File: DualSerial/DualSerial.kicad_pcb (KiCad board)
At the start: 2 copper layers, 99.9 x 99.9 mm, 7 parts, among them J1 IDE_CONNECTOR, J2 CF Adapter Power, J3 Bus_ISA_8bit

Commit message: DualSerial: More WIP on PCB layout.
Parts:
- removed MH1, MH2, MH3, MH4: MH, MountingHole:MountingHole_3.5mm_Pad
- added C1: 0.1uF, Capacitor_THT:C_Disc_D5.1mm_W3.2mm_P5.00mm, F.Cu at (162.6, 73.7)
- added C2: 0.1uF, Capacitor_THT:C_Disc_D5.1mm_W3.2mm_P5.00mm, F.Cu at (114.3, 69.8)
- added C3: 0.1uF, Capacitor_THT:C_Disc_D5.1mm_W3.2mm_P5.00mm, F.Cu at (186.1, 99.1)
- added C4: 0.1uF, Capacitor_THT:C_Disc_D5.1mm_W3.2mm_P5.00mm, F.Cu at (161.9, 48.3)
- added C5: 22uF, Capacitor_THT:CP_Radial_D7.5mm_P2.50mm, F.Cu at (179.1, 127.0)
- added C6: 4.7uF, Capacitor_THT:CP_Radial_D7.5mm_P2.50mm, F.Cu at (183.5, 89.5)
- added C7: 4.7uF, Capacitor_THT:CP_Radial_D7.5mm_P2.50mm, F.Cu at (174.6, 89.5)
- added C8: 0.1uF, Capacitor_THT:C_Disc_D5.1mm_W3.2mm_P5.00mm, F.Cu at (141.6, 48.3)
- added C9: 0.1uF, Capacitor_THT:C_Disc_D5.1mm_W3.2mm_P5.00mm, F.Cu at (181.6, 56.5)
- added CN1: DB9 Male, w_conn_d-sub:DB_9M, F.Cu at (196.7, 118.3)
- added CN2: DB9 Male, w_conn_d-sub:DB_9M, F.Cu at (196.7, 70.3)
- added J3: COM_A_SELECT, 00Custom:PinHeader_3x02_P2.54mm_Vertical, F.Cu at (110.5, 117.5)
- added J4: IRQ_B_SELECT, Connector_PinHeader_2.54mm:PinHeader_2x05_P2.54mm_Vertical, F.Cu at (124.5, 109.9)
- added U1: 16550/16C550, Package_DIP:DIP-40_W15.24mm_Socket, F.Cu at (143.5, 73.7)
- added U2: GAL16V8, Package_DIP:DIP-20_W7.62mm_Socket, F.Cu at (108.0, 73.7)
- added U3: GD75232N, Package_DIP:DIP-20_W7.62mm_Socket, F.Cu at (175.3, 99.1)
- added U4: 1.8432 MHz, 00Custom:Crystal_DIP8_DIP14, F.Cu at (148.6, 49.5)
- added U8: 16550/16C550, Package_DIP:DIP-40_W15.24mm_Socket, F.Cu at (121.9, 48.3)
- added U9: GD75232N, Package_DIP:DIP-20_W7.62mm_Socket, F.Cu at (175.3, 59.7)
- J1: value IDE_CONNECTOR -> COM_A_SELECT; footprint Connector_PinSocket_2.54mm:PinSocket_2x20_P2.54mm_Vertical -> 00Custom:PinHeader_3x02_P2.54mm_Vertical
- J2: value CF Adapter Power -> IRQ_A_SELECT; footprint Connector_PinHeader_2.54mm:PinHeader_1x02_P2.54mm_Vertical -> Connector_PinHeader_2.54mm:PinHeader_2x05_P2.54mm_Vertical
- moved J1 76.0 mm to (110.5, 109.9)
- moved J2 64.7 mm to (133.3, 109.9), turned to 0 degrees
- renumbered J3 to J5
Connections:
- net -5V renamed Net-(J5-Pad5)
- net A10 renamed Net-(J5-Pad52)
- net A11 renamed Net-(J5-Pad51)
- net A12 renamed Net-(J5-Pad50)
- net A13 renamed Net-(J5-Pad49)
- net A14 renamed Net-(J5-Pad48)
- net A15 renamed Net-(J5-Pad47)
- net A16 renamed Net-(J5-Pad46)
- net A17 renamed Net-(J5-Pad45)
- net A18 renamed Net-(J5-Pad44)
- net A19 renamed Net-(J5-Pad43)
- net ALE renamed Net-(J5-Pad28)
- net CLK renamed Net-(J5-Pad20)
- net DRQ1 renamed Net-(J5-Pad18)
- net DRQ2 renamed Net-(J5-Pad6)
- net DRQ3 renamed Net-(J5-Pad16)
- net IOCHRDY renamed Net-(J5-Pad41)
- net IRQ6 renamed Net-(J5-Pad22)
- net OSC renamed Net-(J5-Pad30)
- net TC renamed Net-(J5-Pad27)
- net ~DACK0 renamed Net-(J5-Pad19)
- net ~DACK1 renamed Net-(J5-Pad17)
- net ~DACK2 renamed Net-(J5-Pad26)
- net ~DACK3 renamed Net-(J5-Pad15)
- net ~IO_CH_CK renamed Net-(J5-Pad32)
- net ~MEMR renamed Net-(J5-Pad12)
- net ~MEMW renamed Net-(J5-Pad11)
- J1 pad 1: Net-(J1-Pad1) -> VCC
- J1 pad 3: Net-(J1-Pad3) -> GND
- J1 pad 4: Net-(J1-Pad4) -> VCC
- J1 pad 6: Net-(J1-Pad6) -> GND
- J2 pad 1: VCC -> IRQ2
- J2 pad 2: GND -> Net-(J2-Pad10)
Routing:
- net VCC: track 0.00 -> 751.0 mm, vias 0 -> 3
- net D7: track 0.00 -> 124.2 mm, vias 0 -> 2
- net A00: track 0.00 -> 117.8 mm, vias 0 -> 3
- net +12V: track 0.00 -> 117.3 mm, vias 0 -> 3
- net D6: track 0.00 -> 116.7 mm, vias 0 -> 2
- net D2: track 0.00 -> 115.1 mm, vias 0 -> 4
- net D3: track 0.00 -> 114.3 mm, vias 0 -> 4
- net A01: track 0.00 -> 113.8 mm, vias 0 -> 3
- net D1: track 0.00 -> 113.5 mm, vias 0 -> 3
- net D4: track 0.00 -> 113.1 mm, vias 0 -> 4
- net D5: track 0.00 -> 113.0 mm, vias 0 -> 2
- net A02: track 0.00 -> 109.4 mm, vias 0 -> 3
- net UART_XIN: track 0.00 -> 94.9 mm, vias 0 -> 2
- net -12V: track 0.00 -> 74.6 mm
- net D0: track 0.00 -> 73.4 mm, vias 0 -> 2
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- added copper zone on B.Cu, net GND
- added copper zone on F.Cu, net GND
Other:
- net class Default: clearance 0.2 -> 0.26; trace_width 0.25 -> 0.3
- net class Power added: clearance 0.26, trace_width 0.5, via_dia 1, via_drill 0.6
- net class Power High V added: clearance 0.48, trace_width 0.5, via_dia 1, via_drill 0.6
- net class Serial added: clearance 0.36, trace_width 0.3, via_dia 0.8, via_drill 0.4
- rule trace_clearance: 0.2 -> 0.26
- board text added: "PORT A"
- board text added: "PORT B"

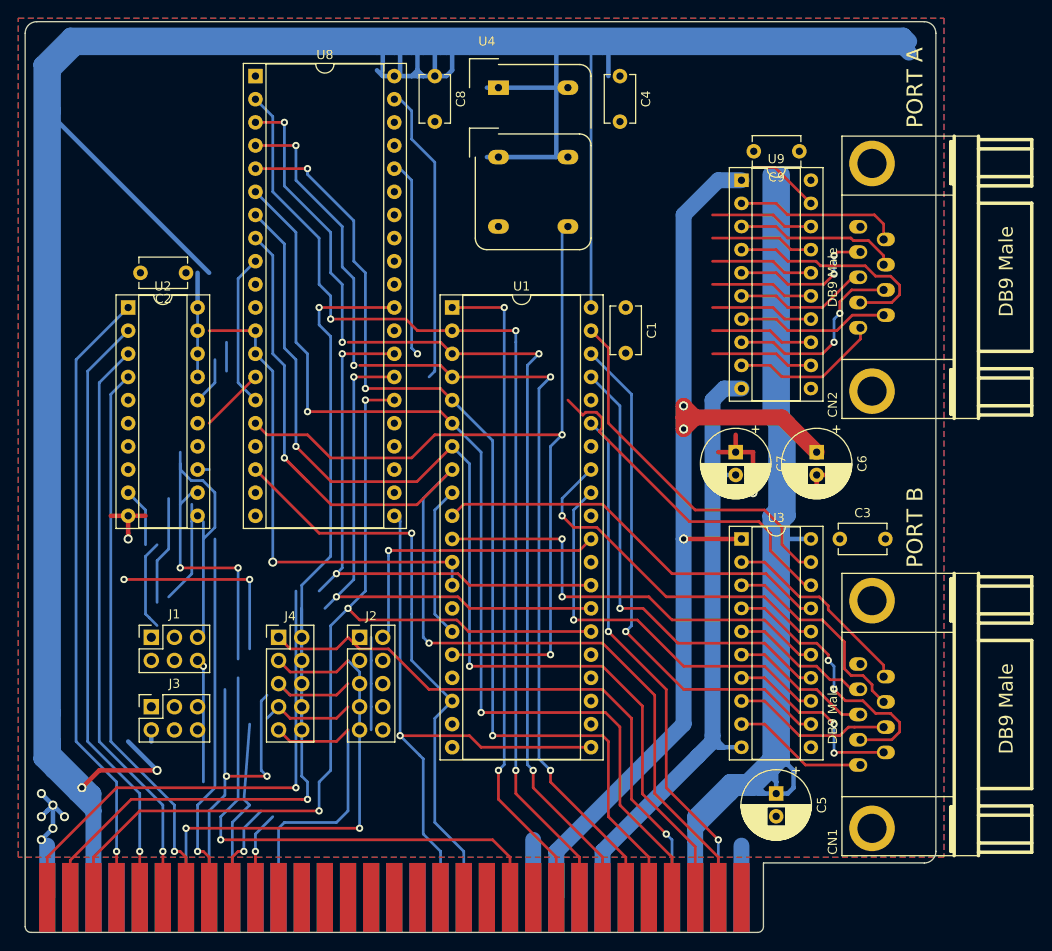
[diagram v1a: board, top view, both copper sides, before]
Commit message: DualSerial: Mostly finished first pass of PCB layout. Still needs component values added and A/B ports are in opposite of desired order.
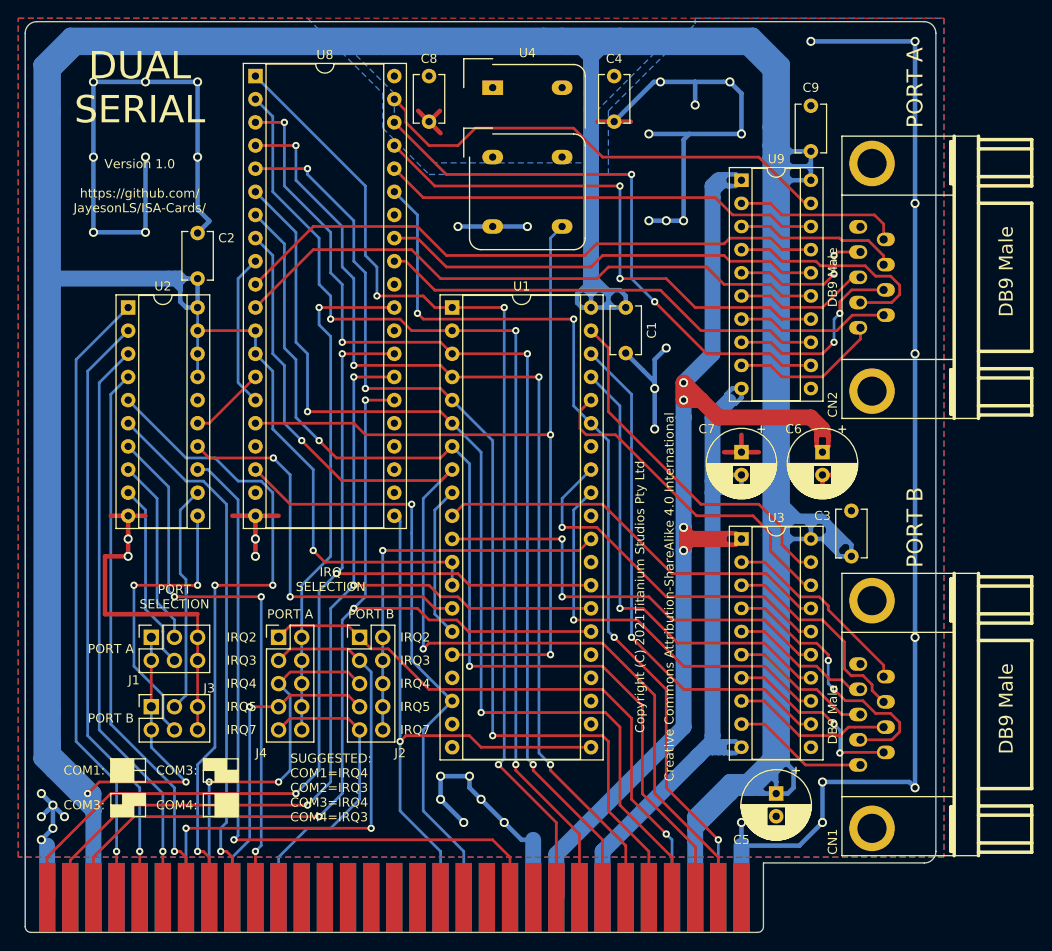
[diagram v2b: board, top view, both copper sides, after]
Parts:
- moved C3 2.29 mm to (187.3, 101.0), turned to 90 degrees
- moved C2 1.42 mm to (115.6, 70.5), turned to 90 degrees
- moved C9 1.27 mm to (182.9, 56.5), turned to 90 degrees
- moved C4 0.64 mm to (161.3, 48.3)
- moved C6 0.64 mm to (184.2, 89.5)
- moved C7 0.63 mm to (175.3, 89.5)
- moved C8 0.63 mm to (141.0, 48.3)
- moved U4 0.63 mm to (148.0, 49.5)
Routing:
- net GND: track 48.7 -> 365.0 mm, vias 8 -> 46
- net VCC: track 751.0 -> 820.0 mm
- net Net-(U8-Pad11): track 11.3 -> 66.7 mm
- net Net-(U8-Pad10): track 11.3 -> 66.2 mm
- net Net-(U8-Pad38): track 11.3 -> 63.5 mm, vias 0 -> 2
- net Net-(U8-Pad37): track 11.3 -> 59.6 mm, vias 0 -> 2
- net +12V: track 117.3 -> 163.9 mm, vias 3 -> 4
- net RESET: track 57.9 -> 101.9 mm, vias 2 -> 4
- net ~UART_A_CS: track 0.00 -> 43.2 mm, vias 0 -> 2
- net Net-(U8-Pad32): track 11.3 -> 50.0 mm
- net D0: track 73.4 -> 111.8 mm, vias 2 -> 3
- net Net-(U8-Pad33): track 11.3 -> 48.4 mm
- net A09: track 31.1 -> 61.4 mm
- net Net-(J3-Pad2): track 2.69 -> 25.1 mm
- net AEN: track 56.8 -> 78.9 mm
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- added copper zone on B.Cu, net VCC
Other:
- board text added: "COM1:"
- board text added: "COM3:"
- board text added: "COM4:"
- board text added: "Copyright (C) 2021Titanium Studios Pty Ltd Creative Commons Attribution-ShareAlike 4.0 International"
- board text added: "DUAL SERIAL"
- board text added: "IRQ SELECTION"
- board text added: "IRQ2"
- board text added: "IRQ3"
- board text added: "IRQ4"
- board text added: "IRQ5"
- board text added: "IRQ7"
- board text added: "PORT SELECTION"
- board text added: "SUGGESTED: COM1=IRQ4 COM2=IRQ3 COM3=IRQ4 COM4=IRQ3"
- board text added: "Version 1.0 https://github.com/ JayesonLS/ISA-Cards/"
